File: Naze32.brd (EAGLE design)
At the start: 35.5 x 35.5 mm, 60 parts, among them IC1 74AHC1G86, J1 USB-MICROB, U3 MPU-65003MM, U4 CP2104SMT, U6 STM32F10XCXT6, U7 BMP280, Y1 12MHz

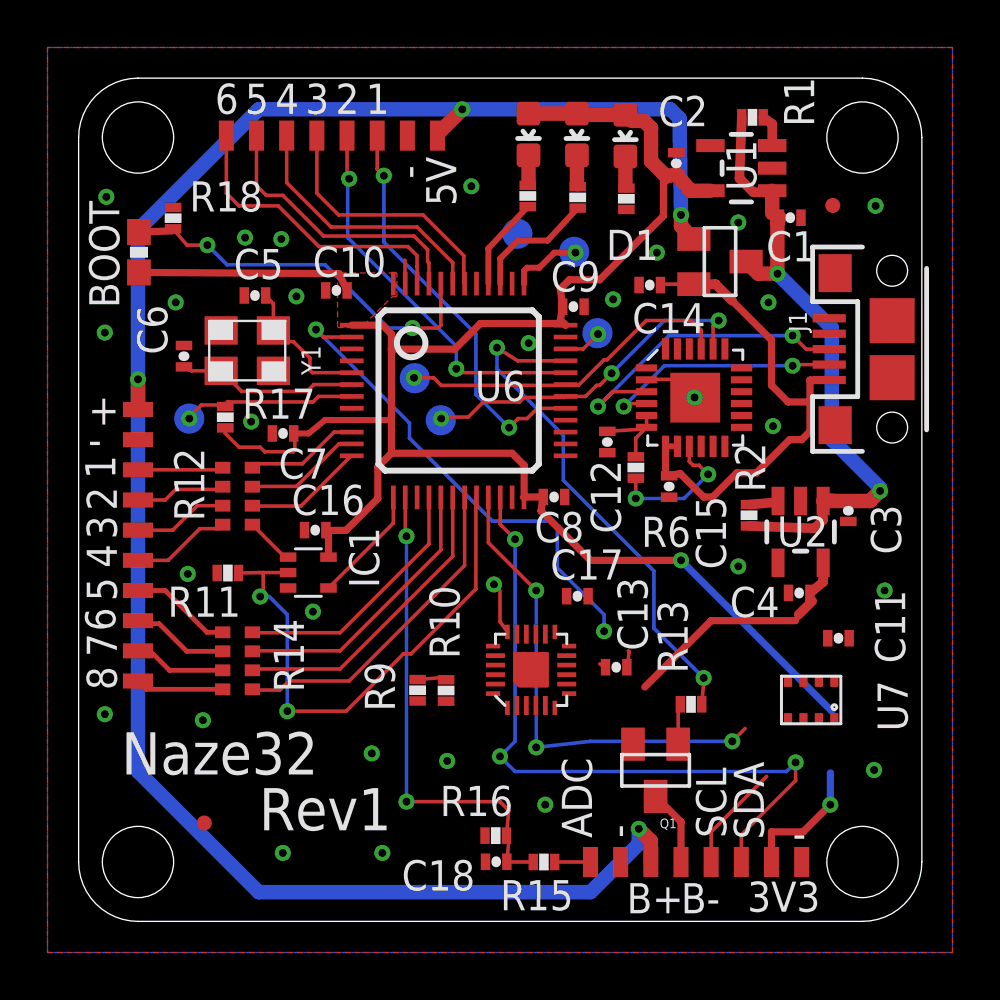
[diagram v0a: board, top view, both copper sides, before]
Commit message: Uploaded complete Naze routing
Uploaded a downrev'd version previously. Updated to the compete version.
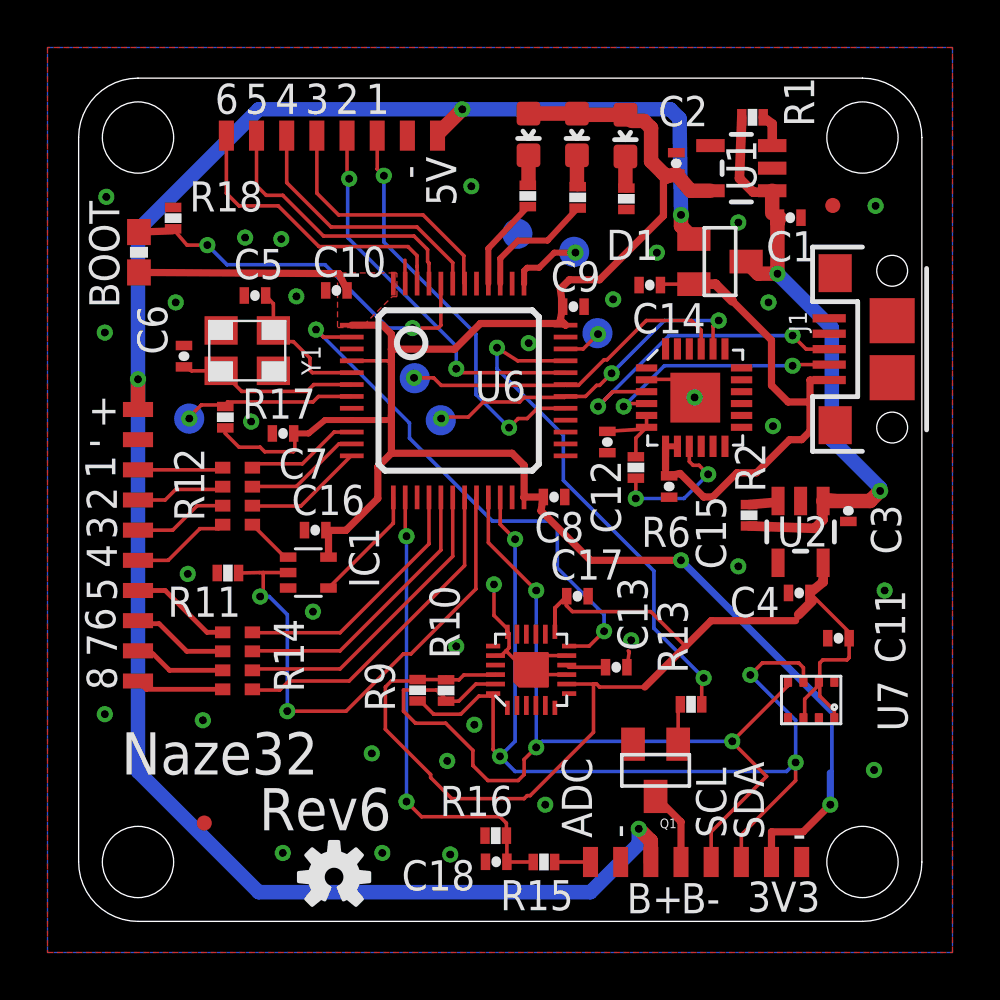
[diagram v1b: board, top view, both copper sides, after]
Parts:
- added U$1: (no value), SparkFun-Aesthetics:OSHW-LOGO-S
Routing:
- net VCC_SEN: track 11.8 -> 52.6 mm
- net SCL: track 25.0 -> 43.3 mm
- net SDA: track 29.4 -> 43.5 mm, vias 3 -> 4
- net GND: track 6.00 -> 12.6 mm, vias 29 -> 33
- net VCC: track 87.4 -> 91.7 mm
- net MPU_INT: track 20.8 -> 22.5 mm
- net N$15: track 0.28 -> 1.67 mm
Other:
- board text added: "Rev6"
- board text removed: "Rev1"
